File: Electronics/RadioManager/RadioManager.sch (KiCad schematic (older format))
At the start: 15 parts

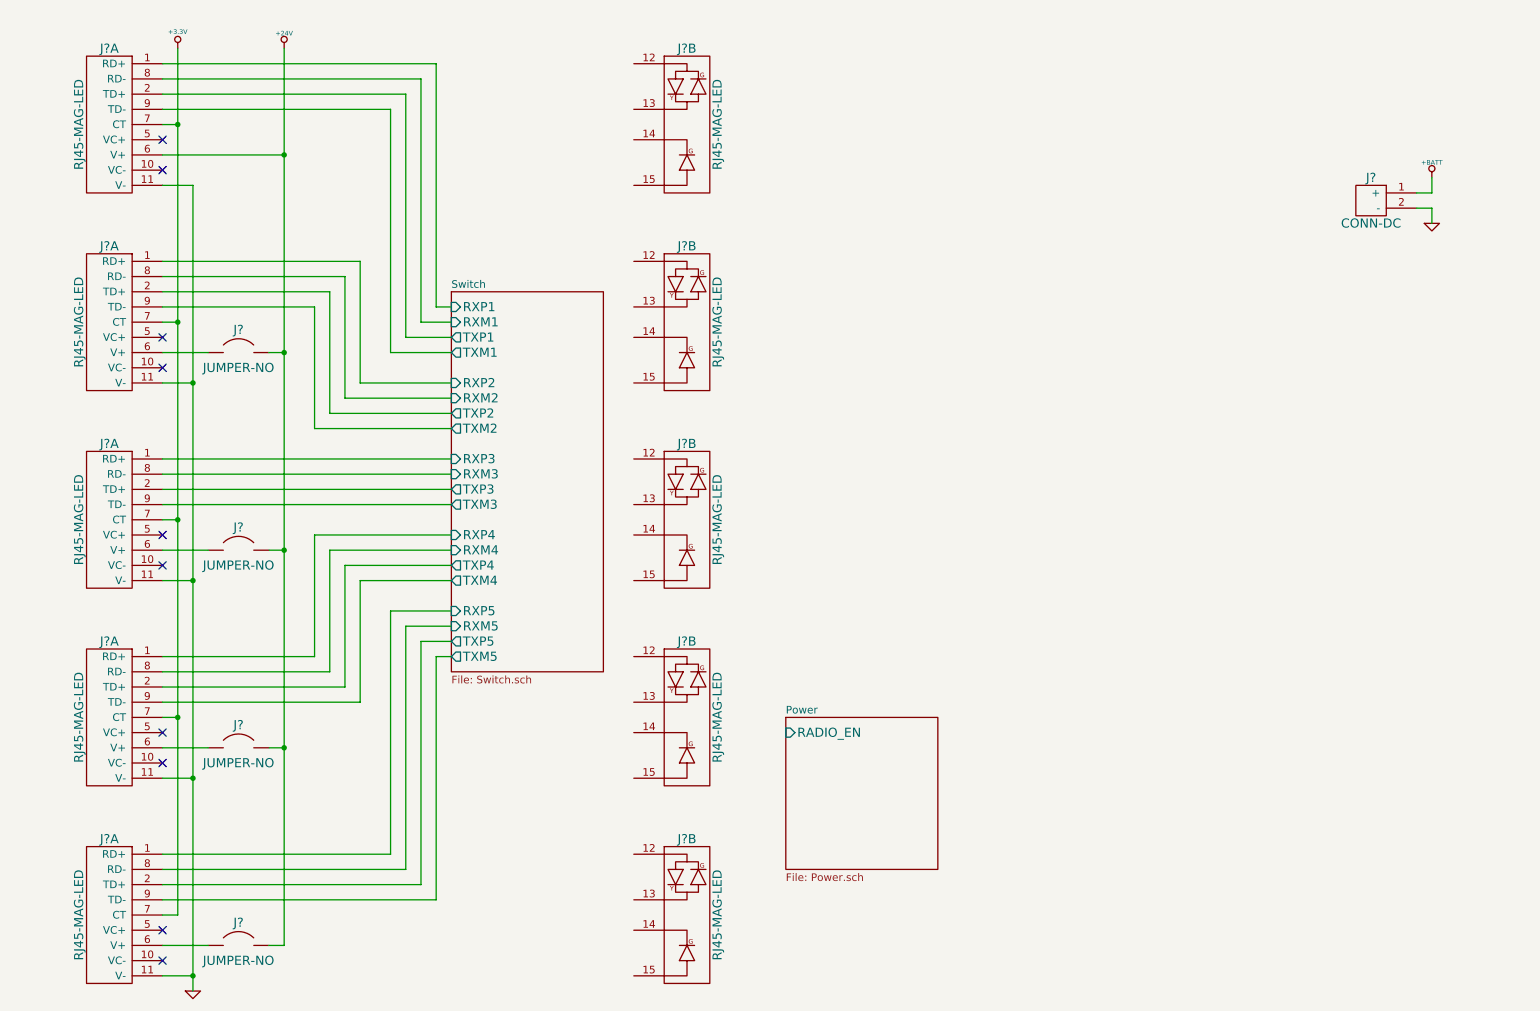
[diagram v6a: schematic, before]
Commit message: Annotate existing components
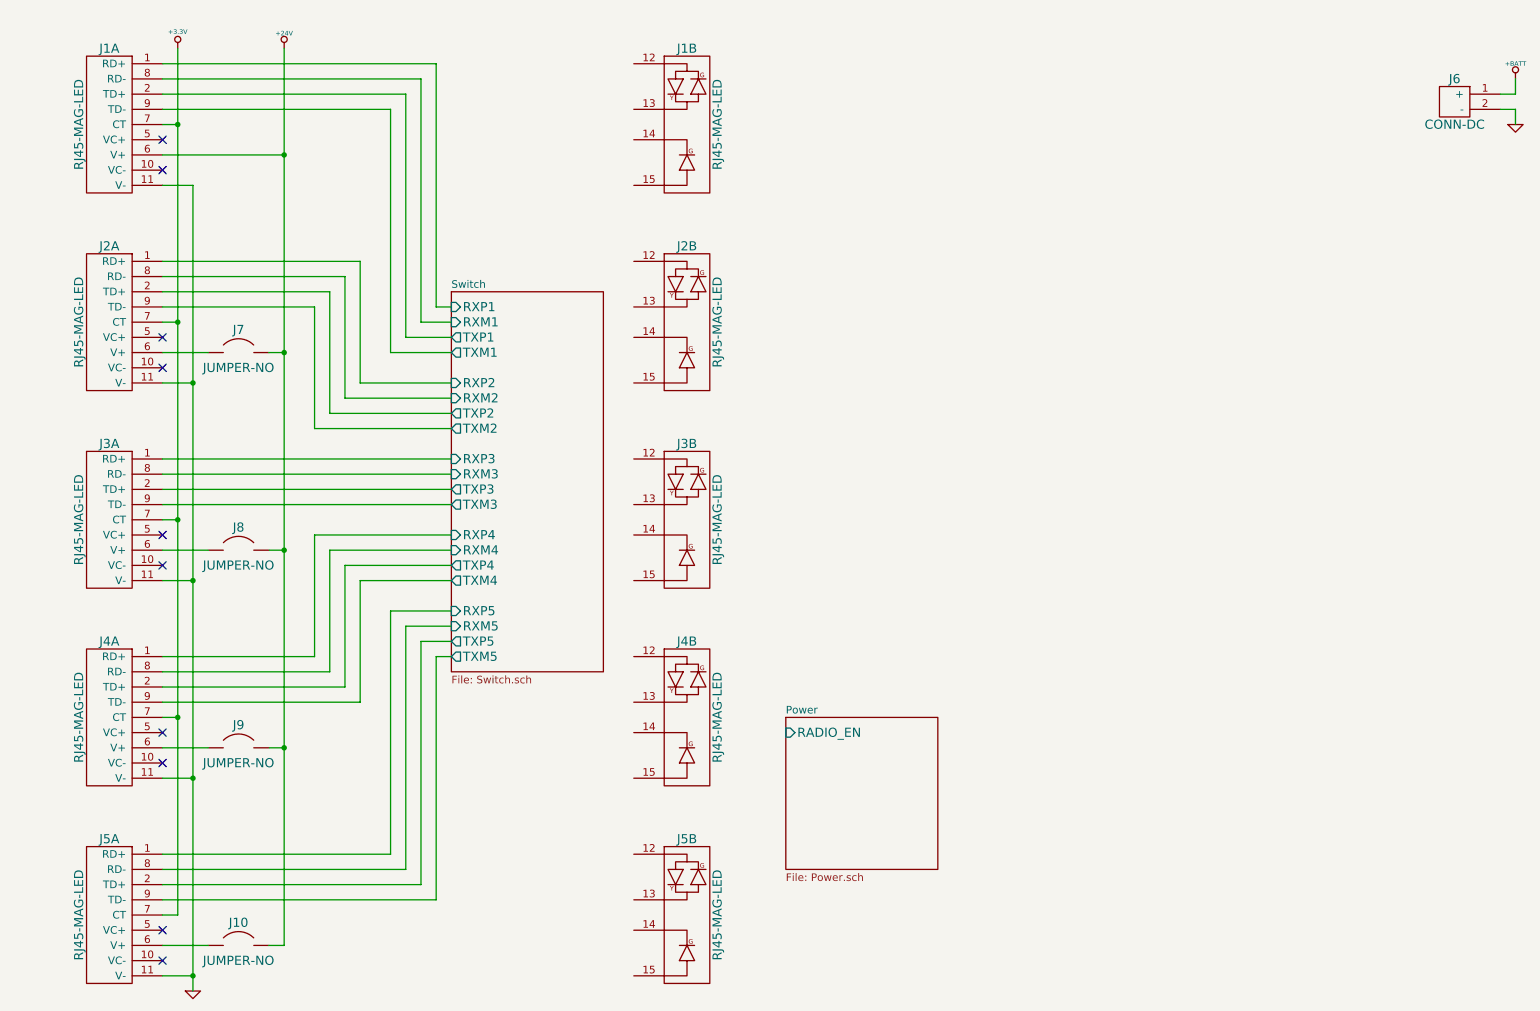
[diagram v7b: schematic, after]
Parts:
- removed J? (x4): JUMPER-NO, ~, symbol JUMPER-NO
- added J10, J7, J8, J9: JUMPER-NO, ~, symbol JUMPER-NO
- gave numbers to parts that had none: 6
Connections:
- net +24V: now also J10.2, J7.2, J8.2, J9.2
- net at J2.6 (V+): now also J7.1
- net at J3.6 (V+): now also J8.1
- net at J4.6 (V+): now also J9.1
- net at J5.6 (V+): now also J10.1
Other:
- moved on the sheet: J6
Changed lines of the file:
@@
 $EndDescr
 $Comp
-L CONN-DC J?
+L CONN-DC J6
 U 1 1 53D1C14A
-P 9450 1900
-F 0 "J?" H 9450 2050 60  0000 C CNN
-F 1 "CONN-DC" H 9450 1750 60  0000 C CNN
-F 2 "~" H 9450 1900 60  0000 C CNN
-F 3 "~" H 9450 1900 60  0000 C CNN
-	1    9450 1900
-	1    0    0    -1
-$EndComp
-$Comp
-L +BATT #PWR?
+P 10000 1250
+F 0 "J6" H 10000 1400 60  0000 C CNN
+F 1 "CONN-DC" H 10000 1100 60  0000 C CNN
+F 2 "~" H 10000 1250 60  0000 C CNN
+F 3 "~" H 10000 1250 60  0000 C CNN
+	1    10000 1250
+	1    0    0    -1
+$EndComp
+$Comp
+L +BATT #PWR4
 U 1 1 53D1C189
-P 9850 1750
-F 0 "#PWR?" H 9850 1700 20  0001 C CNN
-F 1 "+BATT" H 9850 1850 30  0000 C CNN
-F 2 "" H 9850 1750 60  0000 C CNN
-F 3 "" H 9850 1750 60  0000 C CNN
-	1    9850 1750
-	1    0    0    -1
-$EndComp
-$Comp
-L GND #PWR?
+P 10400 1100
+F 0 "#PWR4" H 10400 1050 20  0001 C CNN
+F 1 "+BATT" H 10400 1200 30  0000 C CNN
+F 2 "" H 10400 1100 60  0000 C CNN
+F 3 "" H 10400 1100 60  0000 C CNN
+	1    10400 1100
+	1    0    0    -1
+$EndComp
+$Comp
+L GND #PWR5
 U 1 1 53D1C198
-P 9850 2050
-F 0 "#PWR?" H 9850 2050 30  0001 C CNN
-F 1 "GND" H 9850 1980 30  0001 C CNN
-F 2 "" H 9850 2050 60  0000 C CNN
-F 3 "" H 9850 2050 60  0000 C CNN
-	1    9850 2050
-	1    0    0    -1
-$EndComp
-Wire Wire Line
-	9850 2050 9850 1950
-Wire Wire Line
-	9850 1950 9750 1950
-Wire Wire Line
-	9750 1850 9850 1850
-Wire Wire Line
-	9850 1850 9850 1750
+P 10400 1400
+F 0 "#PWR5" H 10400 1400 30  0001 C CNN
+F 1 "GND" H 10400 1330 30  0001 C CNN
+F 2 "" H 10400 1400 60  0000 C CNN
+F 3 "" H 10400 1400 60  0000 C CNN
+	1    10400 1400
+	1    0    0    -1
+$EndComp
+Wire Wire Line
+	10400 1400 10400 1300
+Wire Wire Line
+	10400 1300 10300 1300
+Wire Wire Line
+	10300 1200 10400 1200
+Wire Wire Line
+	10400 1200 10400 1100
 $Sheet
 S 3400 2500 1000 2500
@@
 $EndSheet
 $Comp
-L RJ45-MAG-LED J?
+L RJ45-MAG-LED J1
 U 1 1 540FBEAD
 P 1150 1400
-F 0 "J?" H 1150 1900 60  0000 C CNN
+F 0 "J1" H 1150 1900 60  0000 C CNN
 F 1 "RJ45-MAG-LED" V 1350 1400 60  0000 C CNN
 F 2 "" H 1150 1400 60  0000 C CNN
@@
 $EndComp
 $Comp
-L RJ45-MAG-LED J?
+L RJ45-MAG-LED J1
 U 2 1 540FBEE7
 P 4950 1400
-F 0 "J?" H 4950 1900 60  0000 C CNN
+F 0 "J1" H 4950 1900 60  0000 C CNN
 F 1 "RJ45-MAG-LED" V 5150 1400 60  0000 C CNN
 F 2 "" H 4950 1400 60  0000 C CNN
@@
 $EndComp
 $Comp
-L RJ45-MAG-LED J?
+L RJ45-MAG-LED J2
 U 1 1 540FBEF8
 P 1150 2700
-F 0 "J?" H 1150 3200 60  0000 C CNN
+F 0 "J2" H 1150 3200 60  0000 C CNN
 F 1 "RJ45-MAG-LED" V 1350 2700 60  0000 C CNN
 F 2 "" H 1150 2700 60  0000 C CNN
@@
 $EndComp
 $Comp
-L RJ45-MAG-LED J?
+L RJ45-MAG-LED J2
 U 2 1 540FBF01
 P 4950 2700
-F 0 "J?" H 4950 3200 60  0000 C CNN
+F 0 "J2" H 4950 3200 60  0000 C CNN
 F 1 "RJ45-MAG-LED" V 5150 2700 60  0000 C CNN
 F 2 "" H 4950 2700 60  0000 C CNN
@@
 $EndComp
 $Comp
-L RJ45-MAG-LED J?
+L RJ45-MAG-LED J3
 U 1 1 540FBF0A
 P 1150 4000
-F 0 "J?" H 1150 4500 60  0000 C CNN
+F 0 "J3" H 1150 4500 60  0000 C CNN
 F 1 "RJ45-MAG-LED" V 1350 4000 60  0000 C CNN
 F 2 "" H 1150 4000 60  0000 C CNN
@@
 $EndComp
 $Comp
-L RJ45-MAG-LED J?
+L RJ45-MAG-LED J3
 U 2 1 540FBF13
 P 4950 4000
-F 0 "J?" H 4950 4500 60  0000 C CNN
+F 0 "J3" H 4950 4500 60  0000 C CNN
 F 1 "RJ45-MAG-LED" V 5150 4000 60  0000 C CNN
 F 2 "" H 4950 4000 60  0000 C CNN
@@
 $EndComp
 $Comp
-L RJ45-MAG-LED J?
+L RJ45-MAG-LED J4
 U 1 1 540FBF1C
 P 1150 5300
-F 0 "J?" H 1150 5800 60  0000 C CNN
+F 0 "J4" H 1150 5800 60  0000 C CNN
 F 1 "RJ45-MAG-LED" V 1350 5300 60  0000 C CNN
 F 2 "" H 1150 5300 60  0000 C CNN
@@
 $EndComp
 $Comp
-L RJ45-MAG-LED J?
+L RJ45-MAG-LED J4
 U 2 1 540FBF25
 P 4950 5300
-F 0 "J?" H 4950 5800 60  0000 C CNN
+F 0 "J4" H 4950 5800 60  0000 C CNN
 F 1 "RJ45-MAG-LED" V 5150 5300 60  0000 C CNN
 F 2 "" H 4950 5300 60  0000 C CNN
@@
 $EndComp
 $Comp
-L RJ45-MAG-LED J?
+L RJ45-MAG-LED J5
 U 1 1 540FBF2E
 P 1150 6600
-F 0 "J?" H 1150 7100 60  0000 C CNN
+F 0 "J5" H 1150 7100 60  0000 C CNN
 F 1 "RJ45-MAG-LED" V 1350 6600 60  0000 C CNN
 F 2 "" H 1150 6600 60  0000 C CNN
@@
 $EndComp
 $Comp
-L RJ45-MAG-LED J?
+L RJ45-MAG-LED J5
 U 2 1 540FBF37
 P 4950 6600
-F 0 "J?" H 4950 7100 60  0000 C CNN
+F 0 "J5" H 4950 7100 60  0000 C CNN
 F 1 "RJ45-MAG-LED" V 5150 6600 60  0000 C CNN
 F 2 "" H 4950 6600 60  0000 C CNN
@@
 	2500 4100 3400 4100
 $Comp
-L +24V #PWR?
+L +24V #PWR3
 U 1 1 5415973E
 P 2300 900
-F 0 "#PWR?" H 2300 850 20  0001 C CNN
+F 0 "#PWR3" H 2300 850 20  0001 C CNN
 F 1 "+24V" H 2300 1000 30  0000 C CNN
 F 2 "" H 2300 900 60  0000 C CNN
@@
 $EndComp
 $Comp
-L +3.3V #PWR?
+L +3.3V #PWR1
 U 1 1 5415A150
 P 1600 900
-F 0 "#PWR?" H 1600 860 30  0001 C CNN
+F 0 "#PWR1" H 1600 860 30  0001 C CNN
 F 1 "+3.3V" H 1600 1010 30  0000 C CNN
 F 2 "" H 1600 900 60  0000 C CNN
@@
 NoConn ~ 1500 6900
 $Comp
-L GND #PWR?
+L GND #PWR2
 U 1 1 5415AF1D
 P 1700 7100
-F 0 "#PWR?" H 1700 7100 30  0001 C CNN
+F 0 "#PWR2" H 1700 7100 30  0001 C CNN
 F 1 "GND" H 1700 7030 30  0001 C CNN
 F 2 "" H 1700 7100 60  0000 C CNN
@@
 	1500 7000 1700 7000
 Connection ~ 1700 7000
-$Comp
-L JUMPER-NO J?
-U 1 1 5415C180
+Wire Wire Line
+	2200 2900 2300 2900
+Wire Wire Line
+	2300 900  2300 6800
+Wire Wire Line
+	2300 6800 2200 6800
+Connection ~ 2300 2900
+Wire Wire Line
+	2200 4200 2300 4200
+Connection ~ 2300 4200
+Wire Wire Line
+	2200 5500 2300 5500
+Connection ~ 2300 5500
+Wire Wire Line
+	1800 6800 1500 6800
+Wire Wire Line
+	1800 5500 1500 5500
+Wire Wire Line
+	1800 4200 1500 4200
+Wire Wire Line
+	1800 2900 1500 2900
+Wire Wire Line
+	1500 1600 2300 1600
+Connection ~ 2300 1600
+$Comp
+L JUMPER-NO J7
+U 1 1 5415EE32
 P 2000 2900
-F 0 "J?" H 2000 3050 60  0000 C CNN
+F 0 "J7" H 2000 3050 60  0000 C CNN
 F 1 "JUMPER-NO" H 2000 2800 60  0000 C CNN
 F 2 "~" H 2000 2900 60  0000 C CNN
@@
 	1    0    0    -1
 $EndComp
-Wire Wire Line
-	2200 2900 2300 2900
-Wire Wire Line
-	2300 900  2300 6800
-$Comp
-L JUMPER-NO J?
-U 1 1 5415C2EC
+$Comp
+L JUMPER-NO J8
+U 1 1 5415EE41
 P 2000 4200
-F 0 "J?" H 2000 4350 60  0000 C CNN
+F 0 "J8" H 2000 4350 60  0000 C CNN
 F 1 "JUMPER-NO" H 2000 4100 60  0000 C CNN
 F 2 "~" H 2000 4200 60  0000 C CNN
@@
 $EndComp
 $Comp
-L JUMPER-NO J?
-U 1 1 5415C379
+L JUMPER-NO J9
+U 1 1 5415EECE
 P 2000 5500
-F 0 "J?" H 2000 5650 60  0000 C CNN
+F 0 "J9" H 2000 5650 60  0000 C CNN
 F 1 "JUMPER-NO" H 2000 5400 60  0000 C CNN
 F 2 "~" H 2000 5500 60  0000 C CNN
@@
 $EndComp
 $Comp
-L JUMPER-NO J?
-U 1 1 5415C388
+L JUMPER-NO J10
+U 1 1 5415EEDD
 P 2000 6800
-F 0 "J?" H 2000 6950 60  0000 C CNN
+F 0 "J10" H 2000 6950 60  0000 C CNN
 F 1 "JUMPER-NO" H 2000 6700 60  0000 C CNN
 F 2 "~" H 2000 6800 60  0000 C CNN
@@
 	1    0    0    -1
 $EndComp
-Wire Wire Line
-	2300 6800 2200 6800
-Connection ~ 2300 2900
-Wire Wire Line
-	2200 4200 2300 4200
-Connection ~ 2300 4200
-Wire Wire Line
-	2200 5500 2300 5500
-Connection ~ 2300 5500
-Wire Wire Line
-	1800 6800 1500 6800
-Wire Wire Line
-	1800 5500 1500 5500
-Wire Wire Line
-	1800 4200 1500 4200
-Wire Wire Line
-	1800 2900 1500 2900
-Wire Wire Line
-	1500 1600 2300 1600
-Connection ~ 2300 1600
 $EndSCHEMATC
